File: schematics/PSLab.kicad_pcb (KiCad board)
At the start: 4 copper layers, 99 x 53.3 mm, 182 parts, among them J1 DoublePins, J11 Li-Ion Battery, J2 Power Pins, J3 Wave Generator, J4 I2C, J5 I2C, J6 ESP01, J7 UART, J9 SPI, P1 SDCard, Q1 MMBT3906, Q2 MMBT3904, Q3 MMBT3906, Q4 Q_NMOS_DGS, SW1 BOOT, SW2 MCLR Reset, SW3 USB_C - Generic, U1 LDFM33PUR, U10 TL082, U11 TL082, U12 MCP4728, U13 MCP6S21, U14 MCP6S21, U15 CP2102N, U16 SP0503BAHT, U18 LTC4040, U19 TC1240A, U2 74HC126, U3 PIC24EP256GP204, U4 DS1307Z+, U5 TC7660, U7 LM324, U8 TL082, U9 TL082, X2 32.768 kHz, Y1 12 MHz

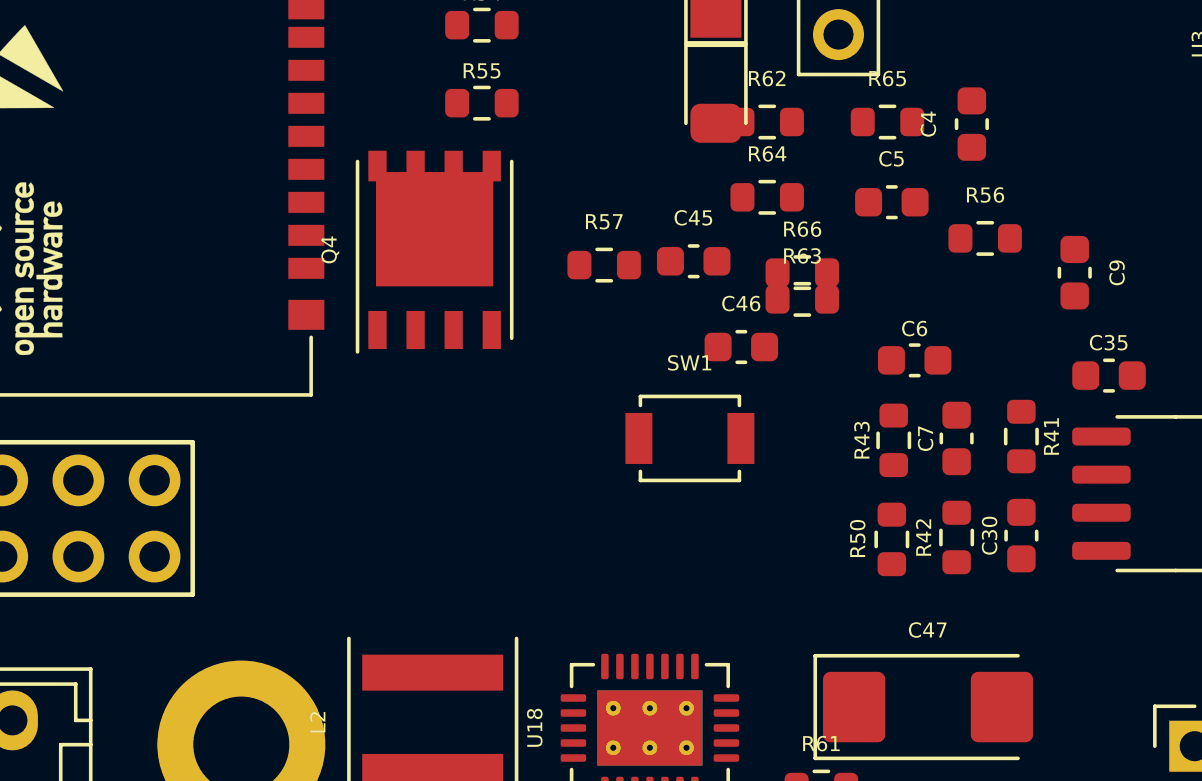
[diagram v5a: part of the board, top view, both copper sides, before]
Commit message: refactor: caps for esp
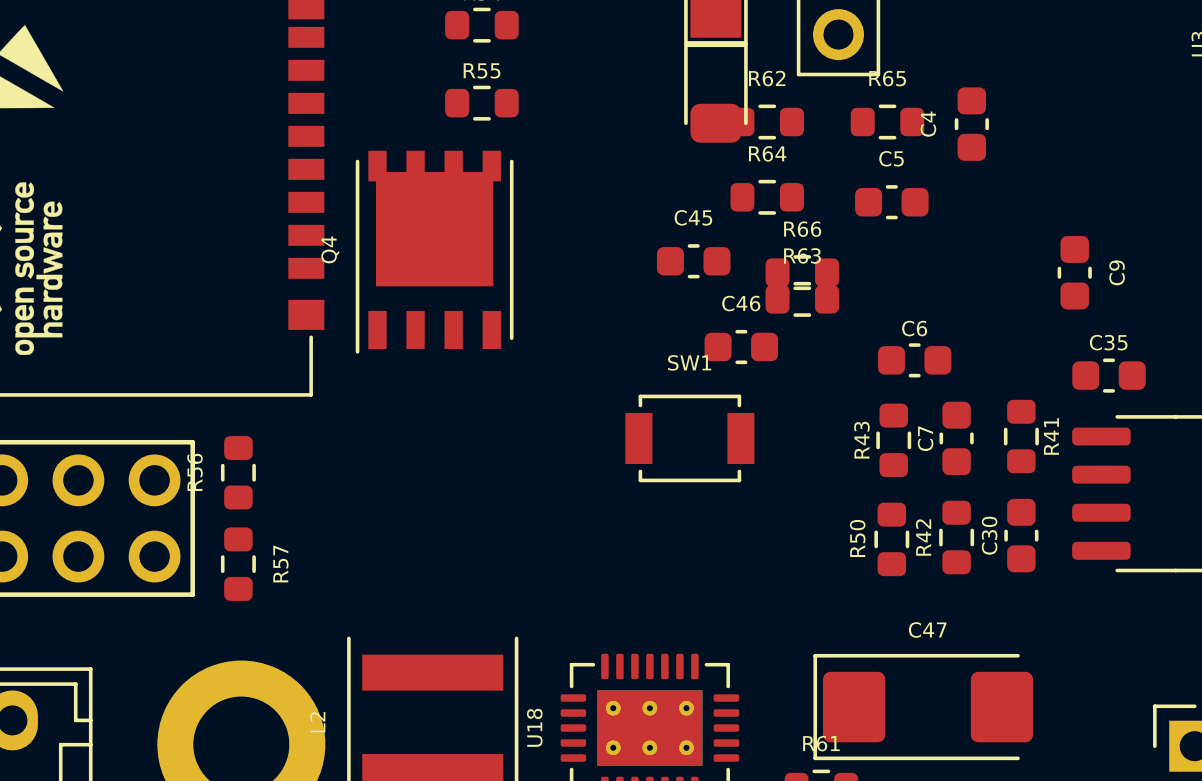
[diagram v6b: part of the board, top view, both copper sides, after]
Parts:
- moved R56 26.1 mm to (104.8, 102.0), turned to 90 degrees
- moved R57 15.7 mm to (104.8, 105.0), turned to 270 degrees
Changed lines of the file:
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@@
   )
   (module Resistor_SMD:R_0603_1608Metric (layer L1.Front)
-    (at 129.675 94.149)
+    (at 104.783 101.9595 90)
     (descr "Resistor SMD 0603 (1608 Metric), square (rectangular) end terminal, IPC_7351 nominal, (Body size source: IPC-SM-782 page 72, https://www.pcb-3d.com/wordpress/wp-content/uploads/ipc-sm-782a_amendment_1_and_2.pdf), generated with kicad-footprint-generator")
     (tags resistor)
     (attr smd)
-    (fp_text reference R56 (at 0 -1.43) (layer F.SilkS)
+    (fp_text reference R56 (at 0 -1.43 90) (layer F.SilkS)
       (effects (font (size 0.5 0.5) (thickness 0.1)))
     )
-    (fp_text value 18 (at 0 1.43) (layer F.Fab)
+    (fp_text value 18 (at 0 1.43 90) (layer F.Fab)
       (effects (font (size 0.5 0.5) (thickness 0.1)))
     )
@@
     (fp_line (start 1.48 -0.73) (end 1.48 0.73) (layer F.CrtYd) (width 0.05))
     (fp_line (start 1.48 0.73) (end -1.48 0.73) (layer F.CrtYd) (width 0.05))
-    (fp_text user %R (at 0 0) (layer F.Fab)
+    (fp_text user %R (at 0 0 90) (layer F.Fab)
       (effects (font (size 0.5 0.5) (thickness 0.1)))
     )
-    (pad 2 smd roundrect (at 0.825 0) (size 0.8 0.95) (layers L1.Front F.Paste F.Mask) (roundrect_rratio 0.25)
+    (pad 2 smd roundrect (at 0.825 0 90) (size 0.8 0.95) (layers L1.Front F.Paste F.Mask) (roundrect_rratio 0.25)
       (net 128 RxD2))
-    (pad 1 smd roundrect (at -0.825 0) (size 0.8 0.95) (layers L1.Front F.Paste F.Mask) (roundrect_rratio 0.25)
+    (pad 1 smd roundrect (at -0.825 0 90) (size 0.8 0.95) (layers L1.Front F.Paste F.Mask) (roundrect_rratio 0.25)
       (net 35 PGC2))
     (model ${KISYS3DMOD}/Resistor_SMD.3dshapes/R_0603_1608Metric.wrl
@@
   )
   (module Resistor_SMD:R_0603_1608Metric (layer L1.Front)
-    (at 116.975 95.038)
+    (at 104.783 105.0075 270)
     (descr "Resistor SMD 0603 (1608 Metric), square (rectangular) end terminal, IPC_7351 nominal, (Body size source: IPC-SM-782 page 72, https://www.pcb-3d.com/wordpress/wp-content/uploads/ipc-sm-782a_amendment_1_and_2.pdf), generated with kicad-footprint-generator")
     (tags resistor)
     (attr smd)
-    (fp_text reference R57 (at 0 -1.43) (layer F.SilkS)
+    (fp_text reference R57 (at 0 -1.43 90) (layer F.SilkS)
       (effects (font (size 0.5 0.5) (thickness 0.1)))
     )
-    (fp_text value 18 (at 0 1.43) (layer F.Fab)
+    (fp_text value 18 (at 0 1.43 90) (layer F.Fab)
       (effects (font (size 0.5 0.5) (thickness 0.1)))
     )
@@
     (fp_line (start 1.48 -0.73) (end 1.48 0.73) (layer F.CrtYd) (width 0.05))
     (fp_line (start 1.48 0.73) (end -1.48 0.73) (layer F.CrtYd) (width 0.05))
-    (fp_text user %R (at 0 0) (layer F.Fab)
+    (fp_text user %R (at 0 0 90) (layer F.Fab)
       (effects (font (size 0.5 0.5) (thickness 0.1)))
     )
-    (pad 2 smd roundrect (at 0.825 0) (size 0.8 0.95) (layers L1.Front F.Paste F.Mask) (roundrect_rratio 0.25)
+    (pad 2 smd roundrect (at 0.825 0 270) (size 0.8 0.95) (layers L1.Front F.Paste F.Mask) (roundrect_rratio 0.25)
       (net 127 TxD2))
-    (pad 1 smd roundrect (at -0.825 0) (size 0.8 0.95) (layers L1.Front F.Paste F.Mask) (roundrect_rratio 0.25)
+    (pad 1 smd roundrect (at -0.825 0 270) (size 0.8 0.95) (layers L1.Front F.Paste F.Mask) (roundrect_rratio 0.25)
       (net 42 PGD2))
     (model ${KISYS3DMOD}/Resistor_SMD.3dshapes/R_0603_1608Metric.wrl

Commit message: refactor: initial routing
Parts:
- Q4: footprint Package_SO:PowerPAK_SO-8_Single -> PSLab:PowerPAK_SO-8_Single
- moved SW1 22.5 mm to (135.5, 84.6), turned to 90 degrees
- moved U19 22.4 mm to (122.7, 80.7)
- moved C2 21.2 mm to (91.8, 103.4), turned to 90 degrees
- moved C14 19.8 mm to (126.7, 82.7), turned to 270 degrees
- moved R62 19.3 mm to (116.3, 108.6)
- moved C9 19.0 mm to (150.5, 101.8), turned to 180 degrees
- moved FID1 16.2 mm to (109.5, 111.9)
- moved R65 16.1 mm to (112.8, 99.0)
- moved R64 16.0 mm to (119.5, 108.6)
- moved C5 14.8 mm to (135.5, 81.1)
- moved D5 13.6 mm to (125.6, 91.4)
- moved C11 12.6 mm to (124.8, 76.8), turned to 0 degrees
- moved C46 12.2 mm to (109.7, 100.6)
- moved R66 12.0 mm to (112.8, 100.6)
- moved R61 11.8 mm to (113.0, 108.6), turned to 180 degrees
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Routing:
- net +3V3: track 0.00 -> 217.3 mm, vias 0 -> 1
- net +5V: track 0.00 -> 172.7 mm, vias 0 -> 5
- net AVSS: track 0.00 -> 145.9 mm, vias 0 -> 78
- net +6V: track 0.00 -> 133.6 mm, vias 0 -> 5
- net VDDA: track 0.00 -> 125.6 mm
- net SCK: track 0.00 -> 118.5 mm, vias 0 -> 4
- net SDO: track 0.00 -> 108.4 mm, vias 0 -> 4
- net -6V: track 0.00 -> 106.6 mm, vias 0 -> 3
- net -10V: track 0.00 -> 98.2 mm, vias 0 -> 2
- net +10V: track 0.00 -> 97.9 mm, vias 0 -> 2
- net SCL: track 0.00 -> 97.4 mm, vias 0 -> 3
- net SDA: track 0.00 -> 87.1 mm, vias 0 -> 3
- net /VINPUT: track 0.00 -> 68.9 mm, vias 0 -> 2
- net SDI: track 0.00 -> 62.4 mm, vias 0 -> 2
- net RxD2: track 0.00 -> 58.4 mm
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- removed copper zone on F.Cu, net /VUSBIN
- removed copper zone on F.Cu, net AVSS
- removed copper zone on F.Cu, net Net-(BT1-Pad1)

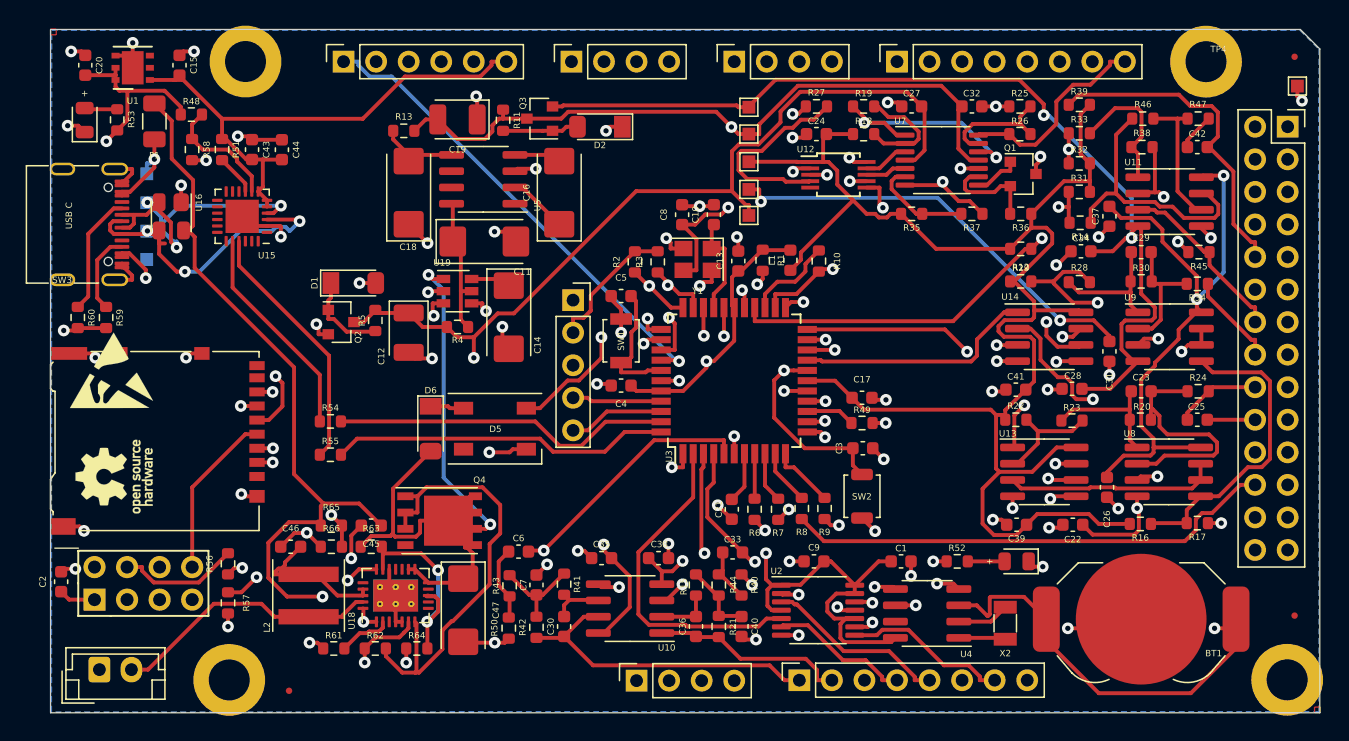
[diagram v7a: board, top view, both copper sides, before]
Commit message: refactor: layout update for osc parts
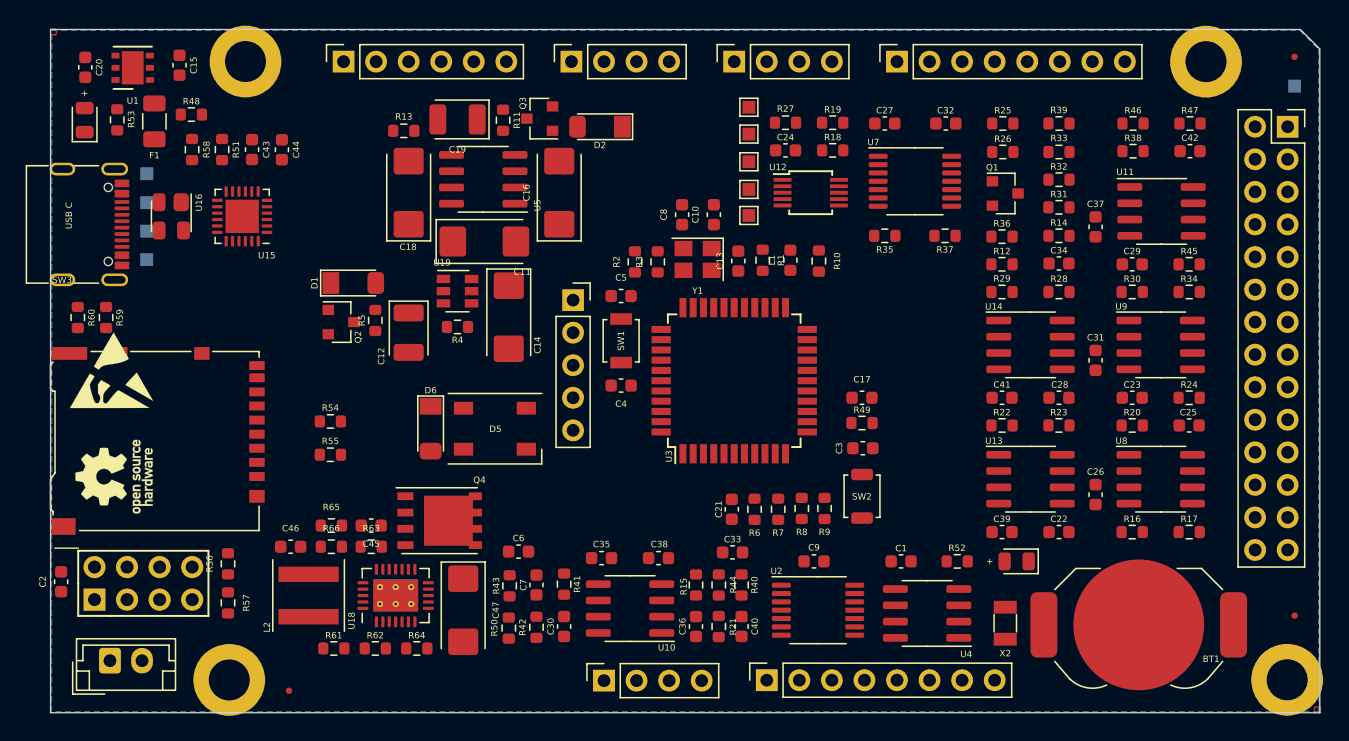
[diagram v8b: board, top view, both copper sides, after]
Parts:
- TP4: moved to B.Cu
- moved R19 2.73 mm to (152.0, 67.5)
- moved R18 2.73 mm to (152.0, 69.7)
- moved R27 2.73 mm to (148.3, 67.5)
- moved C24 2.73 mm to (148.3, 69.7)
- moved R37 2.71 mm to (160.7, 76.4)
- moved R35 2.71 mm to (156.0, 76.4)
- moved U7 2.67 mm to (158.4, 72.1)
- moved U12 2.57 mm to (150.2, 73.0)
- moved J3 2.54 mm to (146.8, 111.0)
- moved J7 2.54 mm to (134.1, 111.1)
- moved C27 2.48 mm to (156.0, 67.6)
- moved C32 2.43 mm to (160.8, 67.6)
- moved R36 2.30 mm to (165.2, 76.4)
- moved R33 2.16 mm to (169.6, 69.8)
- moved R39 2.16 mm to (169.6, 67.6)
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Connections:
- net AVSS renamed GND
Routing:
- net +3V3: track 217.3 -> 0.00 mm, vias 1 -> 0
- net +5V: track 172.7 -> 0.00 mm, vias 5 -> 0
- net GND: track 145.9 -> 0.00 mm, vias 78 -> 0
- net +6V: track 133.6 -> 0.00 mm, vias 5 -> 0
- net VDDA: track 125.6 -> 0.00 mm
- net SCK: track 118.5 -> 0.00 mm, vias 4 -> 0
- net SDO: track 108.4 -> 0.00 mm, vias 4 -> 0
- net -6V: track 106.6 -> 0.00 mm, vias 3 -> 0
- net -10V: track 98.2 -> 0.00 mm, vias 2 -> 0
- net +10V: track 97.9 -> 0.00 mm, vias 2 -> 0
- net SCL: track 97.4 -> 0.00 mm, vias 3 -> 0
- net SDA: track 87.1 -> 0.00 mm, vias 3 -> 0
- net /VINPUT: track 68.9 -> 0.00 mm, vias 2 -> 0
- net SDI: track 62.4 -> 0.00 mm, vias 2 -> 0
- net RxD2: track 58.4 -> 0.00 mm
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- removed copper zone on L3.Power, net Net-(BT1-Pad1)
